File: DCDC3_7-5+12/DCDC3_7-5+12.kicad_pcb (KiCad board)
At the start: 2 copper layers, 63.5 x 75.8 mm, 34 parts, among them J1 FAN, Q1 CSD16323Q3, T1 + 3.7V -, T2 + 12V -, T3 + 5V -, U1 LM3488, U2 XL6009

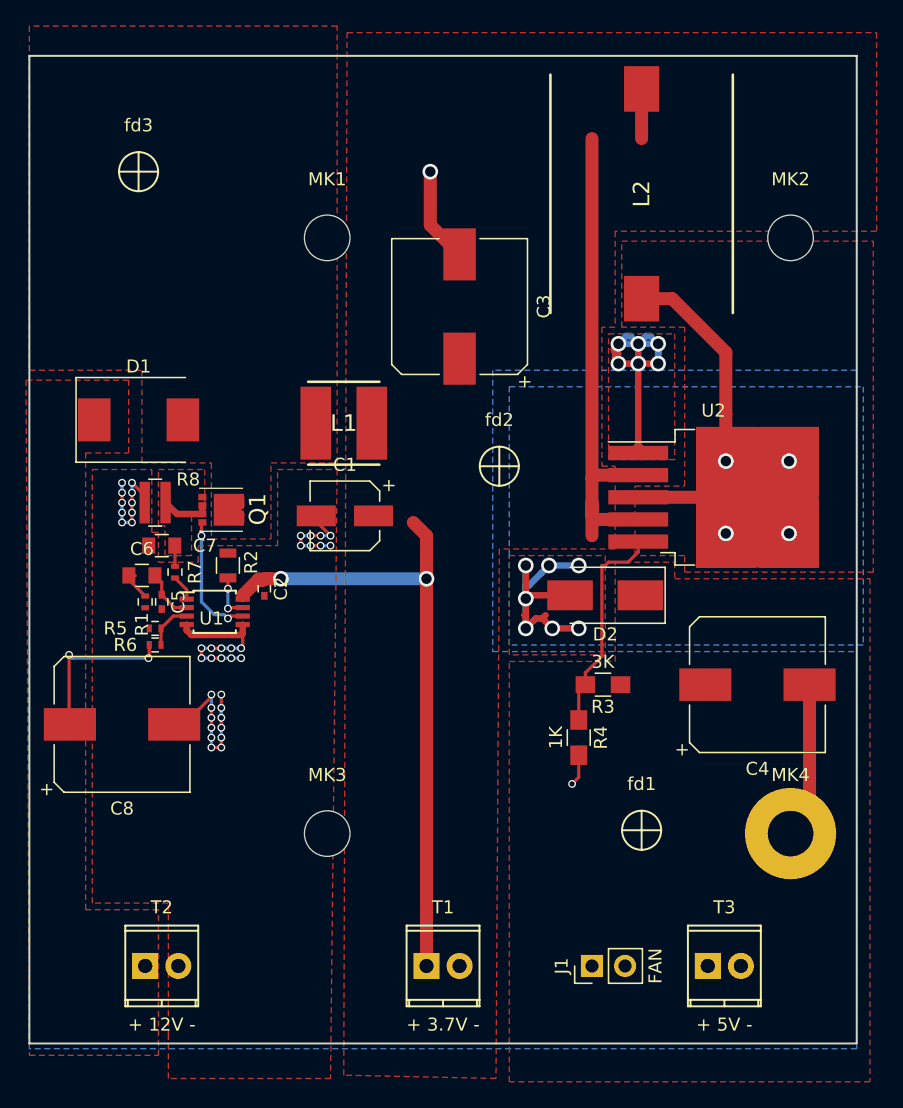
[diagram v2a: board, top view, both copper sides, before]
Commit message: Final version of aux 5v and 12v power supply.
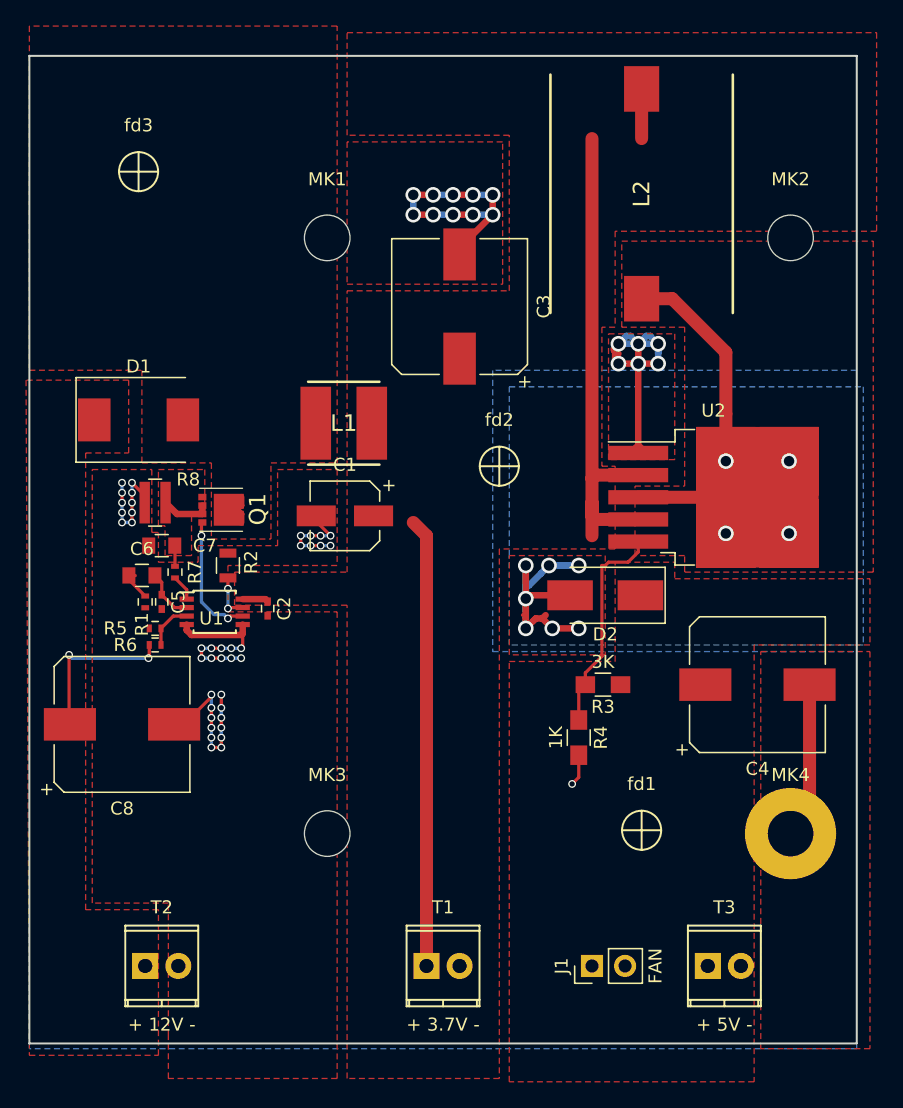
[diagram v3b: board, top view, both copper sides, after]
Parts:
- moved C2 1.55 mm to (119.9, 105.9)
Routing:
- net /DCDC 3.7 - 12/3.7V: track 92.8 -> 79.1 mm, vias 2 -> 0
- net GND: track 87.0 -> 99.1 mm, vias 48 -> 57
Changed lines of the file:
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@@
     (thickness 1.6)
     (drawings 12)
-    (tracks 260)
+    (tracks 267)
     (zones 0)
     (modules 34)
@@
     (47 F.CrtYd user)
     (48 B.Fab user)
-    (49 F.Fab user hide)
+    (49 F.Fab user)
   )
   (setup
@@
   )
   (module Capacitors_SMD:C_0402 (layer F.Cu)
-    (at 119.634 104.394 270)
+    (at 119.888 105.918 270)
     (descr "Capacitor SMD 0402, reflow soldering, AVX (see smccp.pdf)")
     (tags "capacitor 0402")
@@
   (gr_line (start 165.1 63.5) (end 165.1 139.3) (layer Edge.Cuts) (width 0.15))
   (gr_line (start 101.6 63.5) (end 165.1 63.5) (layer Edge.Cuts) (width 0.15))
-  (segment (start 120.904006 103.632) (end 120.904 103.632006) (width 1) (layer B.Cu) (net 1))
-  (segment (start 119.633994 103.632006) (end 120.055472 103.632006) (width 1) (layer F.Cu) (net 1))
-  (segment (start 132.08 103.632) (end 120.904006 103.632) (width 1) (layer B.Cu) (net 1))
-  (via (at 120.904 103.632006) (size 1.2) (drill 0.8) (layers F.Cu B.Cu) (net 1))
-  (segment (start 117.974 104.902) (end 119.152001 103.723999) (width 1) (layer F.Cu) (net 1))
-  (segment (start 120.055472 103.632006) (end 120.904 103.632006) (width 1) (layer F.Cu) (net 1))
-  (segment (start 119.542001 103.723999) (end 119.633994 103.632006) (width 1) (layer F.Cu) (net 1))
-  (segment (start 119.152001 103.723999) (end 119.542001 103.723999) (width 1) (layer F.Cu) (net 1))
-  (segment (start 119.335999 103.723999) (end 119.542001 103.723999) (width 1) (layer F.Cu) (net 1))
-  (segment (start 119.244 103.632) (end 119.335999 103.723999) (width 1) (layer F.Cu) (net 1))
-  (via (at 132.08 103.632) (size 1.2) (drill 0.8) (layers F.Cu B.Cu) (net 1))
-  (segment (start 119.634 103.844) (end 119.456 103.844) (width 0.25) (layer F.Cu) (net 1))
-  (segment (start 119.456 103.844) (end 119.244 103.632) (width 0.25) (layer F.Cu) (net 1))
-  (segment (start 117.974 105.197) (end 117.974 104.902) (width 0.5) (layer F.Cu) (net 1))
+  (segment (start 117.974 105.197) (end 119.717 105.197) (width 0.5) (layer F.Cu) (net 1))
+  (segment (start 119.717 105.197) (end 119.888 105.368) (width 0.5) (layer F.Cu) (net 1))
   (segment (start 132.08 100.33) (end 132.08 103.632) (width 1) (layer F.Cu) (net 1))
   (segment (start 132.08 103.632) (end 132.08 105.41) (width 1) (layer F.Cu) (net 1))
@@
   (segment (start 143.764 114.474) (end 143.764 112.268) (width 0.25) (layer F.Cu) (net 5))
   (segment (start 143.764 112.268) (end 144.272 111.76) (width 0.25) (layer F.Cu) (net 5))
+  (segment (start 137.16 74.168) (end 137.16 75.692) (width 0.5) (layer F.Cu) (net 6))
+  (segment (start 135.636 74.168) (end 137.16 74.168) (width 0.5) (layer B.Cu) (net 6))
+  (via (at 137.16 74.168) (size 1.2) (drill 0.8) (layers F.Cu B.Cu) (net 6))
+  (segment (start 134.112 74.168) (end 135.636 74.168) (width 0.5) (layer F.Cu) (net 6))
+  (via (at 135.636 74.168) (size 1.2) (drill 0.8) (layers F.Cu B.Cu) (net 6))
+  (segment (start 132.588 74.168) (end 134.112 74.168) (width 0.5) (layer B.Cu) (net 6))
+  (via (at 134.112 74.168) (size 1.2) (drill 0.8) (layers F.Cu B.Cu) (net 6))
+  (segment (start 131.064 74.168) (end 132.588 74.168) (width 0.5) (layer F.Cu) (net 6))
+  (via (at 132.588 74.168) (size 1.2) (drill 0.8) (layers F.Cu B.Cu) (net 6))
+  (segment (start 131.064 75.692) (end 131.064 74.168) (width 0.5) (layer B.Cu) (net 6))
+  (via (at 131.064 74.168) (size 1.2) (drill 0.8) (layers F.Cu B.Cu) (net 6))
+  (segment (start 132.588 75.692) (end 131.064 75.692) (width 0.5) (layer F.Cu) (net 6))
+  (via (at 131.064 75.692) (size 1.2) (drill 0.8) (layers F.Cu B.Cu) (net 6))
+  (segment (start 134.112 75.692) (end 132.588 75.692) (width 0.5) (layer B.Cu) (net 6))
+  (via (at 132.588 75.692) (size 1.2) (drill 0.8) (layers F.Cu B.Cu) (net 6))
+  (segment (start 135.636 75.692) (end 134.112 75.692) (width 0.5) (layer F.Cu) (net 6))
+  (via (at 134.112 75.692) (size 1.2) (drill 0.8) (layers F.Cu B.Cu) (net 6))
+  (segment (start 137.16 75.692) (end 135.636 75.692) (width 0.5) (layer B.Cu) (net 6))
+  (via (at 135.636 75.692) (size 1.2) (drill 0.8) (layers F.Cu B.Cu) (net 6))
+  (segment (start 134.62 78.74) (end 134.62 78.232) (width 0.5) (layer F.Cu) (net 6))
+  (segment (start 134.62 78.232) (end 137.16 75.692) (width 0.5) (layer F.Cu) (net 6))
+  (via (at 137.16 75.692) (size 1.2) (drill 0.8) (layers F.Cu B.Cu) (net 6))
   (segment (start 147.736003 84.998003) (end 147.411999 84.998003) (width 0.5) (layer B.Cu) (net 6))
   (segment (start 147.828 85.09) (end 147.736003 84.998003) (width 0.5) (layer B.Cu) (net 6))
@@
   (segment (start 161.48 111.76) (end 161.48 121.73) (width 1) (layer F.Cu) (net 6))
   (segment (start 161.48 121.73) (end 160.02 123.19) (width 1) (layer F.Cu) (net 6))
-  (segment (start 132.37 72.39) (end 132.37 76.49) (width 1) (layer F.Cu) (net 6))
-  (via (at 132.37 72.39) (size 1.2) (drill 0.8) (layers F.Cu B.Cu) (net 6))
-  (segment (start 132.37 76.49) (end 134.62 78.74) (width 1) (layer F.Cu) (net 6))
   (segment (start 148.59 93.98) (end 148.33 93.98) (width 1) (layer F.Cu) (net 6))
   (segment (start 148.33 93.98) (end 148.33 93.72) (width 1) (layer F.Cu) (net 6))
@@
   )
   (zone (net 6) (net_name GND) (layer B.Cu) (hatch edge 0.508)
-    (connect_pads (clearance 0.508))
+    (connect_pads yes (clearance 0.508))
     (min_thickness 0.254)
     (fill yes (arc_segments 16) (thermal_gap 0.508) (thermal_bridge_width 0.508))
@@
         (xy 125.984 61.722) (xy 166.624 61.722) (xy 166.624 76.962) (xy 146.558 76.962) (xy 146.558 84.328)
         (xy 145.542 84.328) (xy 145.542 94.996) (xy 146.558 94.996) (xy 146.558 101.346) (xy 137.668 101.346)
-        (xy 137.414 141.986) (xy 125.73 141.732)
+        (xy 137.668 141.986) (xy 125.984 141.986) (xy 125.984 105.664) (xy 117.348 105.664) (xy 117.348 103.124)
+        (xy 125.984 103.124) (xy 125.984 81.534) (xy 138.43 81.534) (xy 138.43 69.596) (xy 125.984 69.596)
       )
     )
@@
     (polygon
       (pts
-        (xy 166.116 103.632) (xy 166.116 142.24) (xy 138.43 142.24) (xy 138.43 109.982) (xy 146.558 109.982)
-        (xy 146.558 102.362) (xy 151.13 102.362) (xy 151.13 103.632)
+        (xy 166.116 103.632) (xy 166.116 108.712) (xy 157.226 108.712) (xy 157.226 142.24) (xy 138.43 142.24)
+        (xy 138.43 109.982) (xy 146.558 109.982) (xy 146.558 102.362) (xy 151.13 102.362) (xy 151.13 103.632)
       )
     )
@@
     (polygon
       (pts
-        (xy 125.222 95.25) (xy 124.714 141.986) (xy 112.268 141.986) (xy 112.268 138.684) (xy 112.268 128.524)
-        (xy 106.426 128.524) (xy 106.426 95.25) (xy 110.998 95.25) (xy 110.998 100.076) (xy 111.506 100.076)
-        (xy 111.506 102.362) (xy 114.554 102.362) (xy 114.554 101.092) (xy 120.65 101.092) (xy 120.65 95.25)
+        (xy 125.222 95.25) (xy 125.222 102.616) (xy 116.84 102.616) (xy 116.84 106.172) (xy 125.222 106.172)
+        (xy 125.222 141.986) (xy 112.268 141.986) (xy 112.268 138.684) (xy 112.268 128.524) (xy 106.426 128.524)
+        (xy 106.426 95.25) (xy 110.998 95.25) (xy 110.998 100.076) (xy 111.506 100.076) (xy 111.506 102.362)
+        (xy 114.554 102.362) (xy 114.554 101.092) (xy 120.65 101.092) (xy 120.65 95.25)
       )
     )
@@
       )
     )
+  )
+  (zone (net 6) (net_name GND) (layer F.Cu) (hatch edge 0.508)
+    (connect_pads yes (clearance 0.508))
+    (min_thickness 0.254)
+    (fill yes (arc_segments 16) (thermal_gap 0.508) (thermal_bridge_width 0.508))
+    (polygon
+      (pts
+        (xy 157.734 109.22) (xy 166.116 109.22) (xy 166.116 139.7) (xy 157.734 139.7)
+      )
+    )
+  )
+  (zone (net 6) (net_name GND) (layer F.Cu) (hatch edge 0.508)
+    (connect_pads yes (clearance 0.508))
+    (min_thickness 0.254)
+    (fill yes (arc_segments 16) (thermal_gap 0.508) (thermal_bridge_width 0.508))
+    (polygon
+      (pts
+        (xy 137.922 81.026) (xy 137.922 70.104) (xy 125.984 70.104) (xy 125.984 81.026)
+      )
+    )

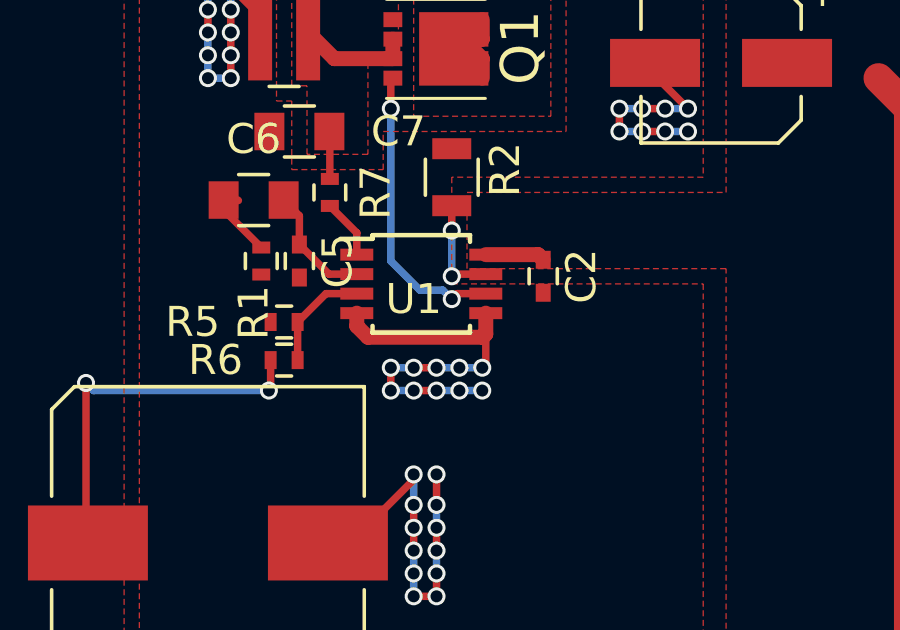
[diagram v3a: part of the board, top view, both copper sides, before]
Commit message: Final version of aux 5v and 12v power supply.
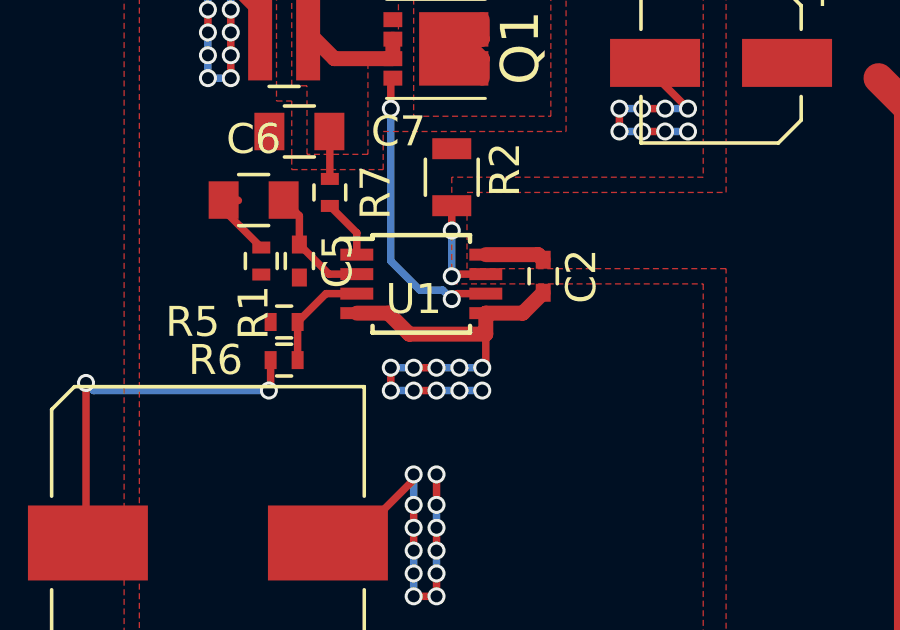
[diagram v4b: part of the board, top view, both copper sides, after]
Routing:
- net GND: track 99.1 -> 100.9 mm
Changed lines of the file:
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@@
     (thickness 1.6)
     (drawings 12)
-    (tracks 267)
+    (tracks 268)
     (zones 0)
     (modules 34)
@@
   (segment (start 143.764 114.474) (end 143.764 112.268) (width 0.25) (layer F.Cu) (net 5))
   (segment (start 143.764 112.268) (end 144.272 111.76) (width 0.25) (layer F.Cu) (net 5))
+  (segment (start 113.674 107.147) (end 114.724 107.147) (width 0.5) (layer F.Cu) (net 6))
+  (segment (start 114.724 107.147) (end 115.424 107.847) (width 0.5) (layer F.Cu) (net 6))
+  (segment (start 115.424 107.847) (end 117.974 107.847) (width 0.5) (layer F.Cu) (net 6))
+  (segment (start 117.974 107.147) (end 119.209 107.147) (width 0.5) (layer F.Cu) (net 6))
+  (segment (start 119.209 107.147) (end 119.888 106.468) (width 0.5) (layer F.Cu) (net 6))
   (segment (start 137.16 74.168) (end 137.16 75.692) (width 0.5) (layer F.Cu) (net 6))
   (segment (start 135.636 74.168) (end 137.16 74.168) (width 0.5) (layer B.Cu) (net 6))
@@
   (segment (start 110.452 97.244) (end 109.474 96.266) (width 0.25) (layer F.Cu) (net 6))
   (via (at 109.474 96.266) (size 0.6) (drill 0.4) (layers F.Cu B.Cu) (net 6))
-  (segment (start 113.674 107.147) (end 113.674 107.578) (width 0.5) (layer F.Cu) (net 6))
-  (segment (start 117.871 107.95) (end 117.974 107.847) (width 0.5) (layer F.Cu) (net 6))
-  (segment (start 113.674 107.578) (end 114.046 107.95) (width 0.5) (layer F.Cu) (net 6))
-  (segment (start 114.046 107.95) (end 117.871 107.95) (width 0.5) (layer F.Cu) (net 6))
   (segment (start 117.974 107.847) (end 117.974 107.147) (width 0.5) (layer F.Cu) (net 6))
   (segment (start 143.764 117.174) (end 143.764 118.872) (width 0.25) (layer F.Cu) (net 6))
